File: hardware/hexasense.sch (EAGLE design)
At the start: 22 parts, among them IC1 AT45DB161D-SU

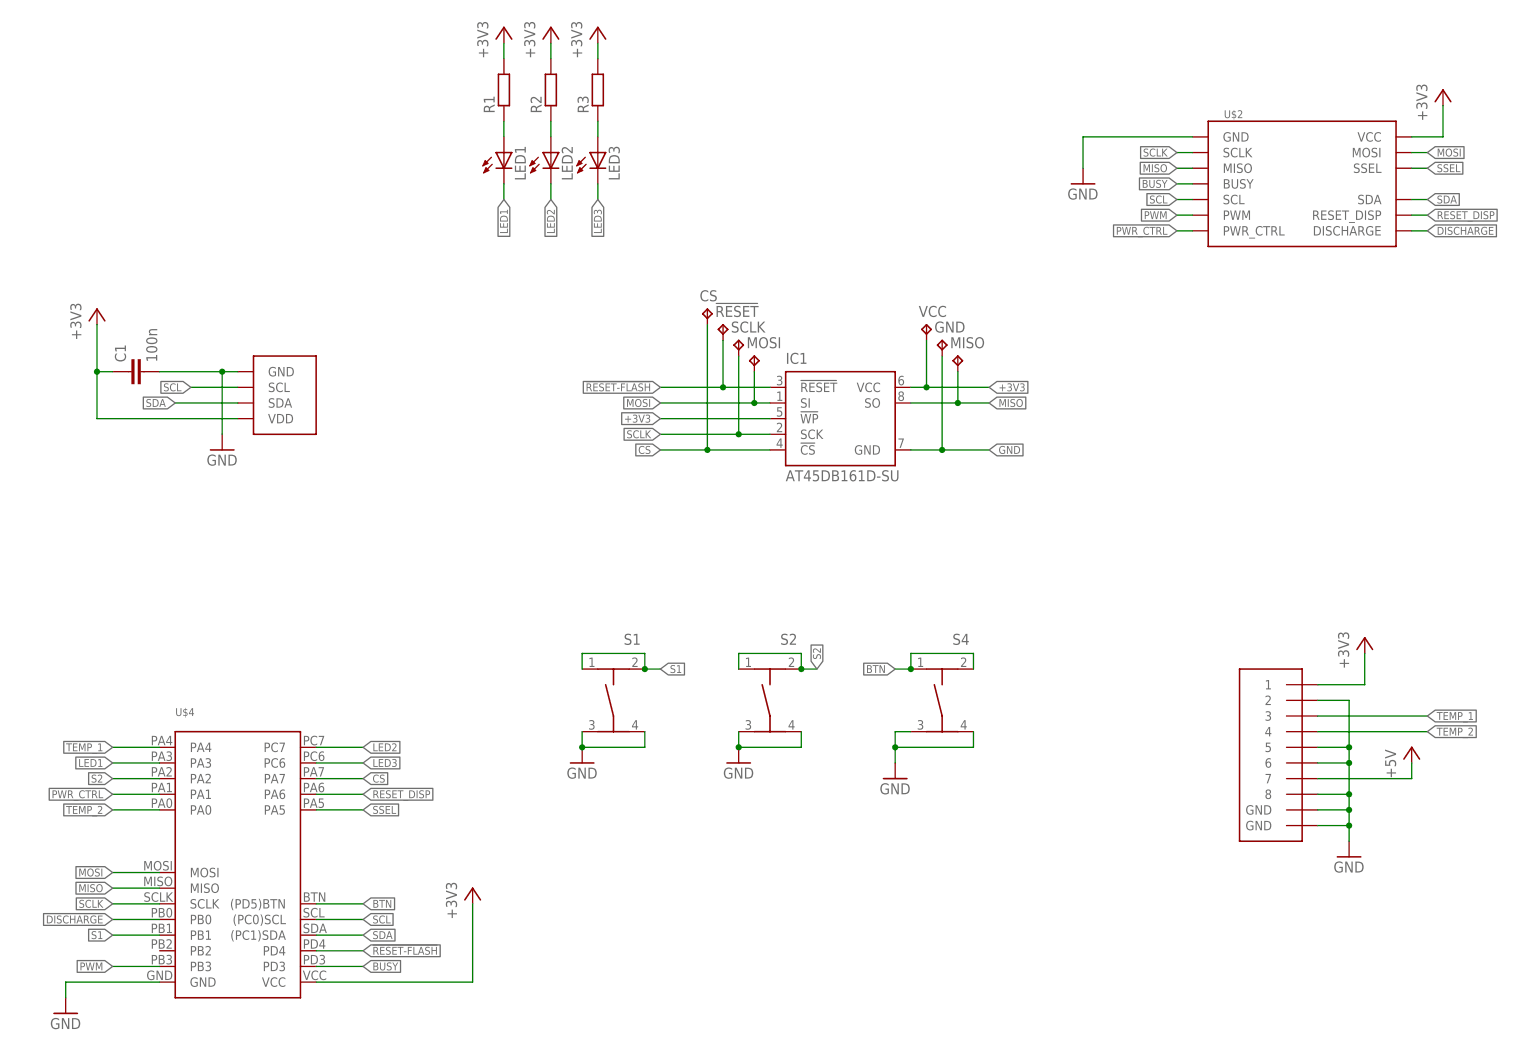
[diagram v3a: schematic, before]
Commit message: connected BORDER_CTRL
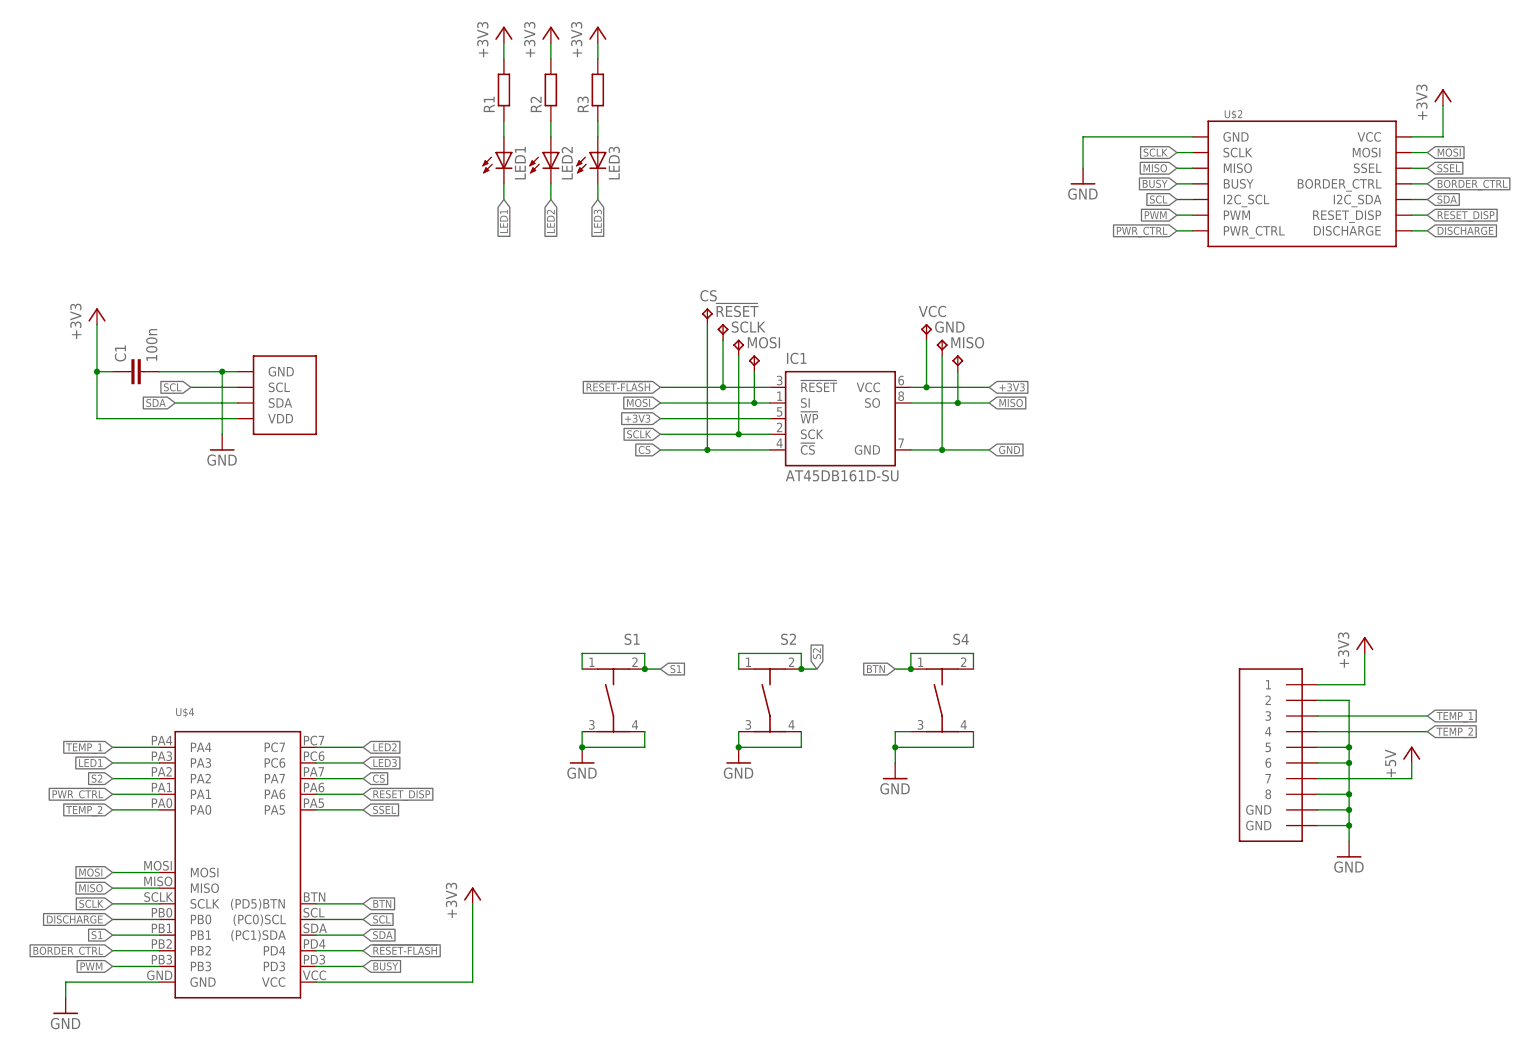
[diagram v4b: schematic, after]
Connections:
- new net BORDER_CTRL: U$2.BORDER_CTRL, U$4.PB2
- net SCL: now also U$2.I2C_SCL; no longer U$2.SCL
- net SDA: now also U$2.I2C_SDA; no longer U$2.SDA
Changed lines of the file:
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@@
 </segment>
 <segment>
-<pinref part="U$2" gate="G$1" pin="SDA"/>
+<pinref part="U$2" gate="G$1" pin="I2C_SDA"/>
 <wire x1="231.14" y1="139.7" x2="233.68" y2="139.7" width="0.1524" layer="91"/>
 <label x="233.68" y="139.7" size="1.27" layer="95" xref="yes"/>
@@
 </segment>
 <segment>
-<pinref part="U$2" gate="G$1" pin="SCL"/>
+<pinref part="U$2" gate="G$1" pin="I2C_SCL"/>
 <wire x1="195.58" y1="139.7" x2="193.04" y2="139.7" width="0.1524" layer="91"/>
 <label x="193.04" y="139.7" size="1.27" layer="95" rot="R180" xref="yes"/>
@@
 </segment>
 </net>
+<net name="BORDER_CTRL" class="0">
+<segment>
+<pinref part="U$2" gate="G$1" pin="BORDER_CTRL"/>
+<wire x1="231.14" y1="142.24" x2="233.68" y2="142.24" width="0.1524" layer="91"/>
+<label x="233.68" y="142.24" size="1.27" layer="95" xref="yes"/>
+</segment>
+<segment>
+<pinref part="U$4" gate="G$1" pin="PB2"/>
+<wire x1="27.94" y1="17.78" x2="20.32" y2="17.78" width="0.1524" layer="91"/>
+<label x="20.32" y="17.78" size="1.27" layer="95" rot="R180" xref="yes"/>
+</segment>
+</net>
